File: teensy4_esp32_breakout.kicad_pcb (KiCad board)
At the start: 2 copper layers, 30.5 x 22.9 mm, 16 parts, among them J1 Conn_01x08, J2 Conn_02x05_Odd_Even, SW1 ON_OFF, U1 ESP32-WROOM-32D, U2 TLV75533PDBV

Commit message: Forgot to save
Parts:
- renumbered 3.3v to JP1
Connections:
- U1 pad 39: GND -> (no net)
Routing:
- net GND: vias 10 -> 9
- net /SCK: vias 2 -> 1
- net (no net): vias 0 -> 1

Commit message: Ordered this board with fix to remove double via and ground the BFV under ESP32
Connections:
- U1 pad 39: (no net) -> GND
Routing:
- net GND: vias 9 -> 10
- net (no net): vias 1 -> 0
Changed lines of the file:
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@@
     (fp_line (start -9.12 -15.865) (end -9.12 -9.445) (layer F.SilkS) (width 0.12))
     (fp_line (start -9.12 -9.445) (end -9.5 -9.445) (layer F.SilkS) (width 0.12))
-    (pad 39 smd rect (at -1 -0.755 270) (size 5 5) (layers F.Cu F.Paste F.Mask))
+    (pad 39 smd rect (at -1 -0.755 270) (size 5 5) (layers F.Cu F.Paste F.Mask)
+      (net 1 GND))
     (pad 1 smd rect (at -8.5 -8.255 270) (size 2 0.9) (layers F.Cu F.Paste F.Mask)
       (net 1 GND))
@@
   (gr_line (start 181.61 100.33) (end 181.61 123.19) (layer Edge.Cuts) (width 0.05))
   (gr_line (start 151.13 100.33) (end 181.61 100.33) (layer Edge.Cuts) (width 0.05))
-  (via (at 173.228 112.014) (size 4.318) (drill 3.81) (layers F.Cu B.Cu) (net 0) (status 30))
+  (via (at 173.228 112.014) (size 4.318) (drill 3.81) (layers F.Cu B.Cu) (net 1) (status 30))
   (segment (start 154.94 101.6) (end 155.067 101.6) (width 0.4572) (layer B.Cu) (net 1) (status 30))
   (segment (start 156.337 102.997) (end 154.94 101.6) (width 0.4572) (layer B.Cu) (net 1) (status 20))

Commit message: fix regulator part number
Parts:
- U2: value TLV75533PDBV -> TLV75733PDBVR
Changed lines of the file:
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@@
     (46 B.CrtYd user)
     (47 F.CrtYd user)
-    (48 B.Fab user hide)
-    (49 F.Fab user hide)
+    (48 B.Fab user)
+    (49 F.Fab user)
   )
   (setup
@@
     (add_net /MISO)
     (add_net /MOSI)
+    (add_net /PROGRAM)
     (add_net /SCK)
     (add_net GND)
@@
     (add_net "Net-(R2-Pad2)")
     (add_net "Net-(R3-Pad2)")
+    (add_net "Net-(U1-Pad14)")
+    (add_net "Net-(U1-Pad16)")
+    (add_net "Net-(U1-Pad17)")
+    (add_net "Net-(U1-Pad18)")
+    (add_net "Net-(U1-Pad19)")
+    (add_net "Net-(U1-Pad20)")
+    (add_net "Net-(U1-Pad21)")
+    (add_net "Net-(U1-Pad22)")
+    (add_net "Net-(U1-Pad23)")
+    (add_net "Net-(U1-Pad26)")
+    (add_net "Net-(U1-Pad27)")
+    (add_net "Net-(U1-Pad28)")
+    (add_net "Net-(U1-Pad31)")
+    (add_net "Net-(U1-Pad32)")
+    (add_net "Net-(U1-Pad33)")
+    (add_net "Net-(U1-Pad4)")
+    (add_net "Net-(U1-Pad5)")
+    (add_net "Net-(U1-Pad6)")
+    (add_net "Net-(U1-Pad7)")
+    (add_net "Net-(U1-Pad8)")
+    (add_net "Net-(U1-Pad9)")
+    (add_net "Net-(U2-Pad4)")
   )
   (module RF_Module:ESP32-WROOM-32 (layer F.Cu)
@@
       (effects (font (size 1 1) (thickness 0.15)))
     )
-    (fp_text value TLV75533PDBV (at 0 2.9) (layer F.Fab)
-      (effects (font (size 1 1) (thickness 0.15)))
-    )
+    (fp_text value TLV75733PDBVR (at 0 2.9) (layer F.Fab)
+      (effects (font (size 1 1) (thickness 0.15)))
+    )

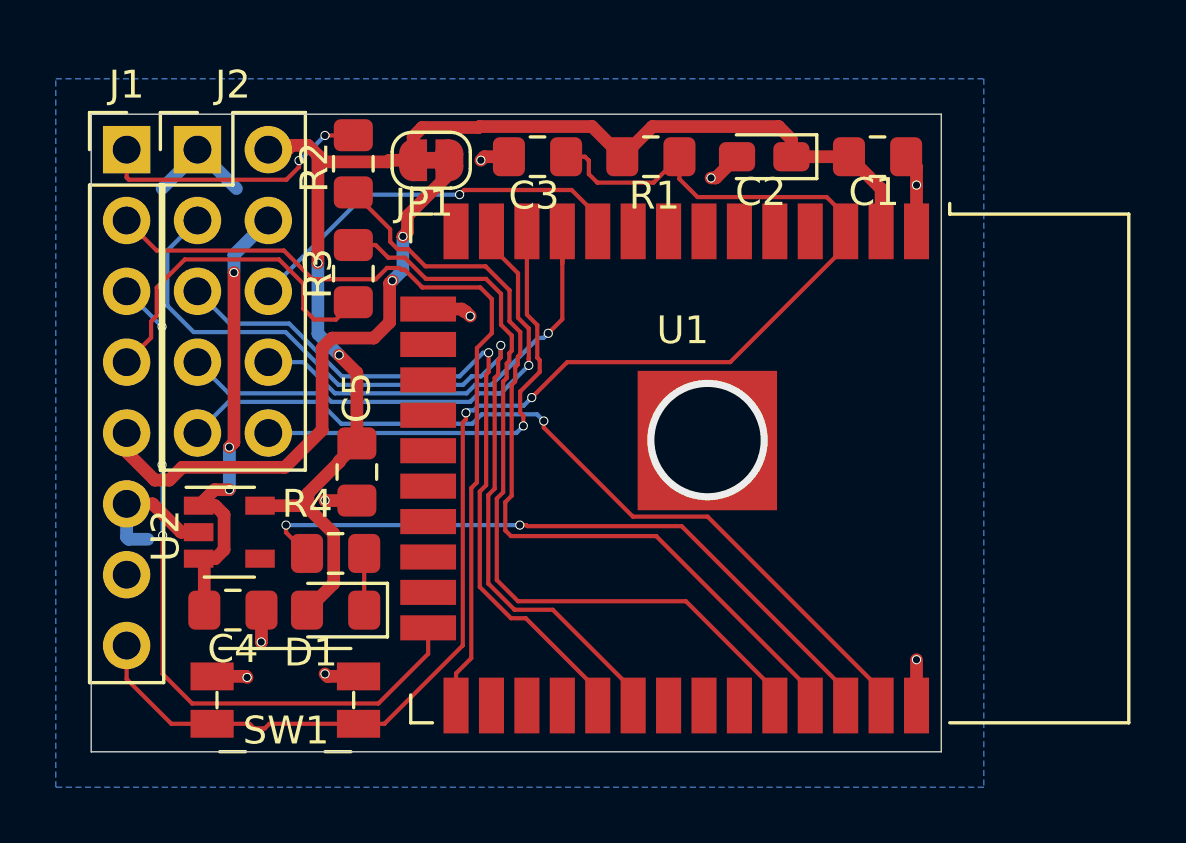
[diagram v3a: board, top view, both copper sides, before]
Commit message: Added two more pins from ESP32 to header, including pin used for ESP_BUSY by WiFiNINA
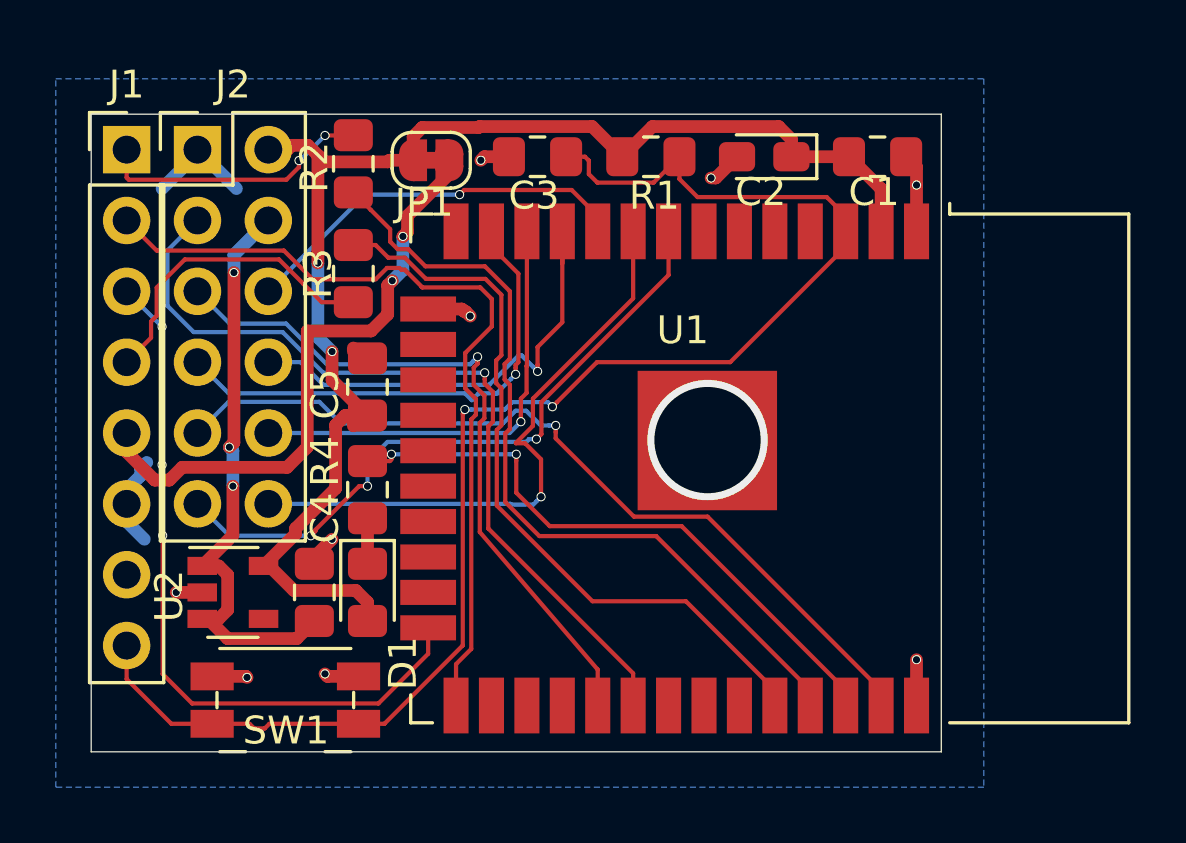
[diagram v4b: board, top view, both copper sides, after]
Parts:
- J2: value Conn_02x05_Odd_Even -> Conn_02x06_Odd_Even; footprint Connector_PinHeader_2.54mm:PinHeader_2x05_P2.54mm_Vertical -> Connector_PinHeader_2.54mm:PinHeader_2x06_P2.54mm_Vertical
- moved C5 3.07 mm to (161.0, 110.1), turned to 90 degrees
- moved C4 2.99 mm to (159.1, 117.5), turned to 90 degrees
- moved R4 2.56 mm to (161.0, 113.8), turned to 270 degrees
- moved U2 2.16 mm to (156.2, 117.5)
- moved D1 1.31 mm to (161.0, 117.5), turned to 270 degrees
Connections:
- U1 pad 8: (no net) -> /ESP_BUSY
- U1 pad 9: (no net) -> /IO33
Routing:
- net /ESP_BUSY: track 0.00 -> 24.0 mm, vias 0 -> 3
- net /IO33: track 0.00 -> 21.7 mm, vias 0 -> 1
- net /+5V: track 16.8 -> 21.4 mm
- net /SCK: track 33.5 -> 30.1 mm
- net +3V3: track 47.1 -> 49.8 mm
- net /IO22: track 24.4 -> 22.2 mm
- net Net-(R3-Pad2): track 28.8 -> 27.1 mm
- net /CS: track 26.9 -> 25.6 mm
- net GND: track 22.7 -> 21.6 mm
- net /24_TX6: track 12.3 -> 11.2 mm
- net /IO26: track 16.6 -> 17.4 mm
- net Net-(R2-Pad2): track 30.2 -> 29.4 mm
- net /IO27: track 16.8 -> 16.1 mm
- net /3V3_Teensy: track 21.3 -> 21.8 mm
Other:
- board text added: "3.3v 5v IO25 IO26 IO27 NC"
- board text added: "GND SCK CS MOSI MISO BUSY"
- board text added: "RX6 IO0 IO2 TX6 3.3v GND PGM ON/OFF"
- board text removed: "3.3v 5v IO25 IO26 IO27"
- board text removed: "GND SCK CS MOSI MISO"
- board text removed: "RX6 IO0 IO2 TX6 3.3v GND NC ON/OFF"

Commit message: Forgot to save
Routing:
- net /IO26: track 17.4 -> 16.6 mm
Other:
- board text added: "3.3v 5v IO25 IO26 IO27 IO33"
- board text added: "Teensy 4.0 ESP32 Breakout 2019-09-25"
- board text removed: "3.3v 5v IO25 IO26 IO27 NC"
- board text removed: "Teensy 4.0 ESP32 Breakout 2019-09-24"

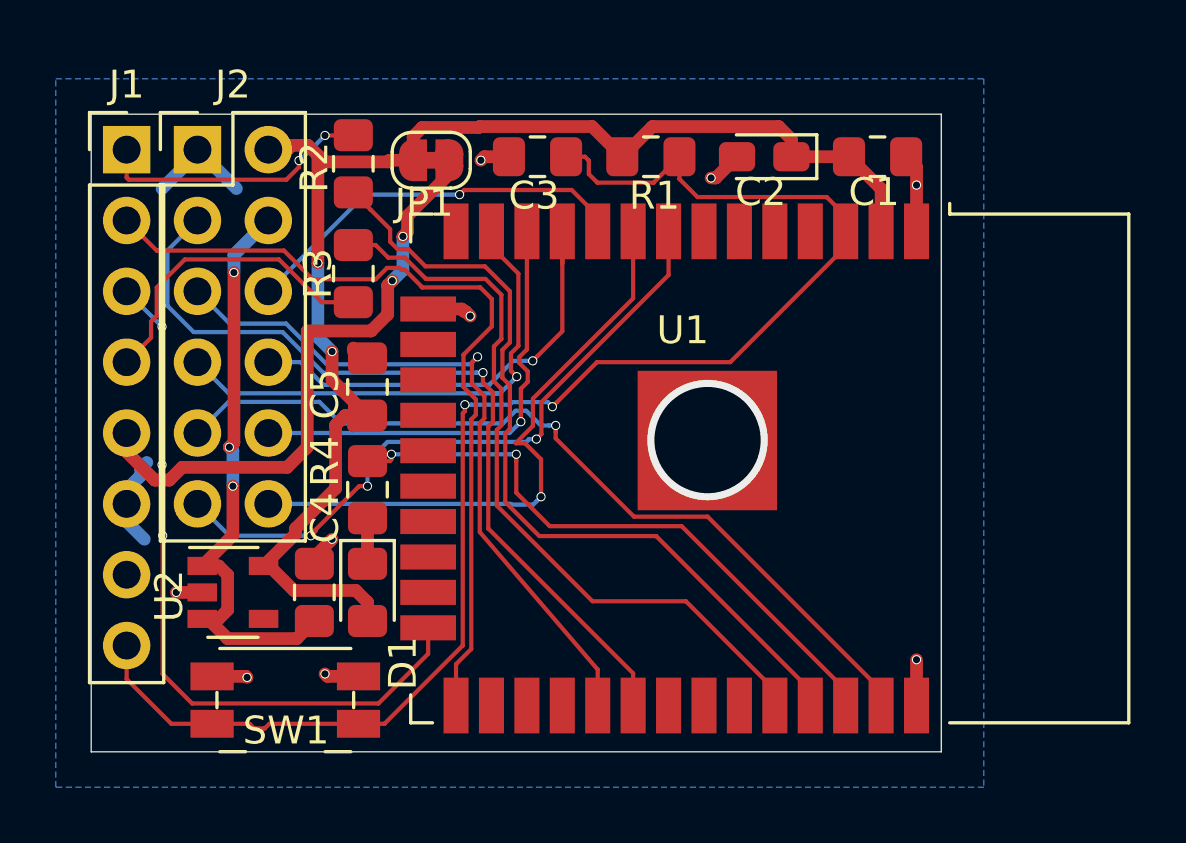
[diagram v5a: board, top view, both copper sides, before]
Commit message: Fix missing wire, update silkscreen & readme
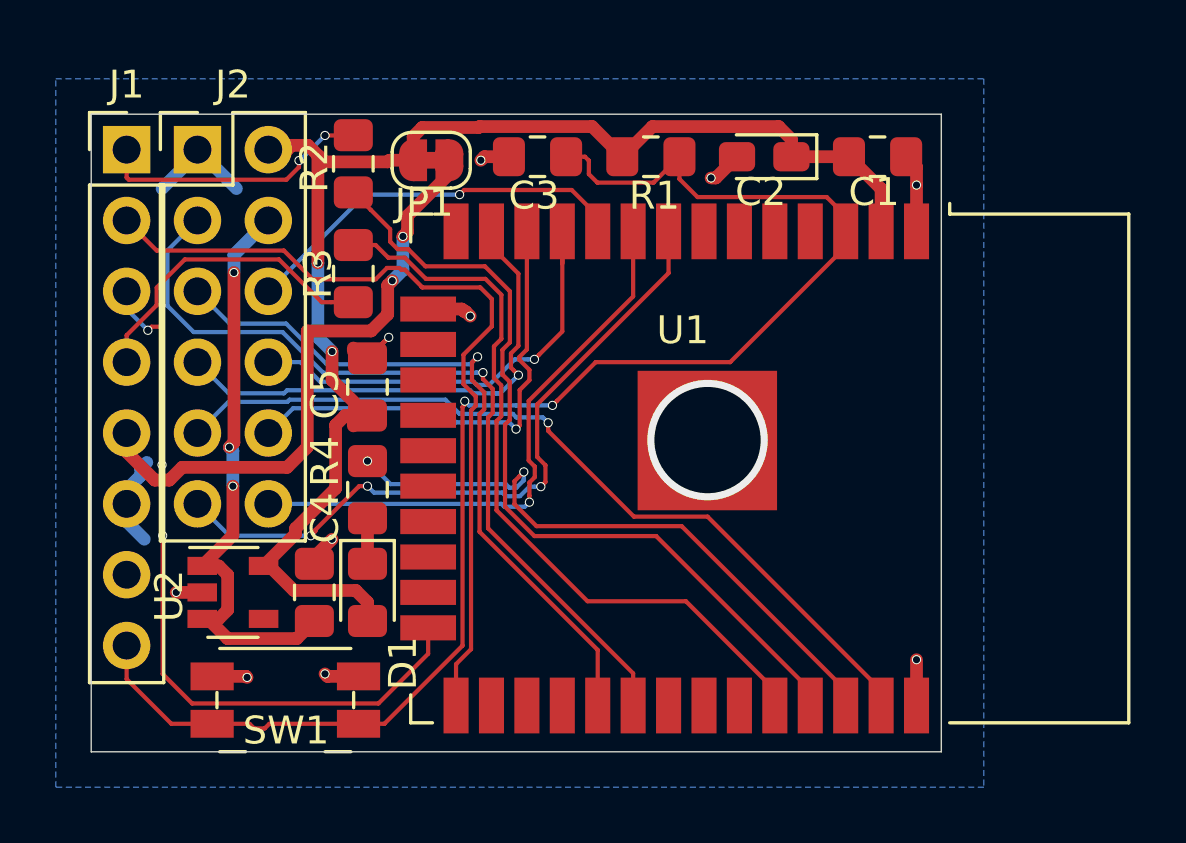
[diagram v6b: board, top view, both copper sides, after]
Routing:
- net GND: track 21.6 -> 24.1 mm, vias 10 -> 11
- net /ESP_BUSY: track 24.0 -> 25.1 mm
- net /IO33: track 21.7 -> 20.9 mm
- net /IO27: track 16.4 -> 17.1 mm
- net /IO22: track 22.2 -> 22.9 mm
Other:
- board text added: "RX6 IO0 IO2 TX6 3.3v GND PGM RESET"
- board text removed: "RX6 IO0 IO2 TX6 3.3v GND PGM ON/OFF"

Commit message: Updates to remove program/on_off pin connections
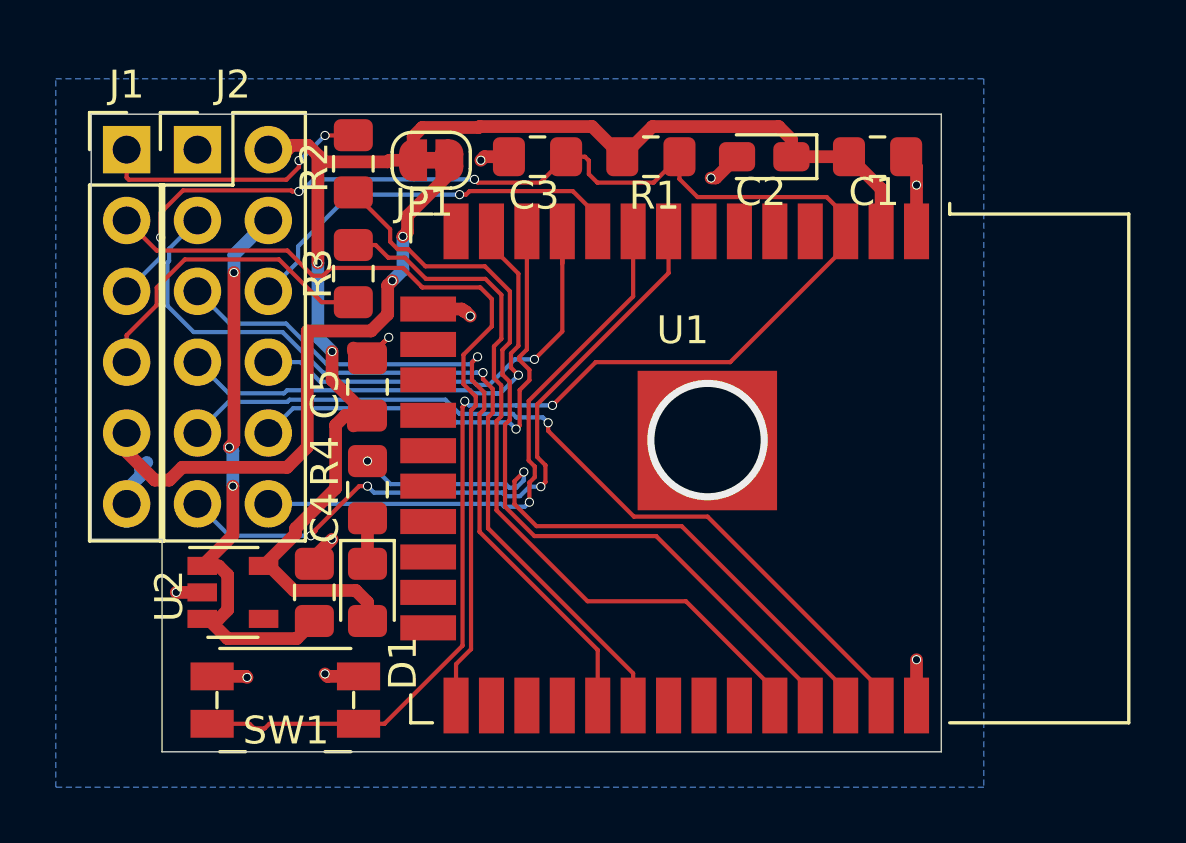
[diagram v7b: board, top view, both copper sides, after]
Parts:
- J1: value Conn_01x08 -> Conn_01x06; footprint Connector_PinHeader_2.54mm:PinHeader_1x08_P2.54mm_Vertical -> Connector_PinHeader_2.54mm:PinHeader_1x06_P2.54mm_Vertical
- SW1: value ON_OFF -> RESET
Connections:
- net /26 renamed /26_IO0
- C3 pad 1: /ESP32_EN -> /28_EN
- J1 pad 3: /28 -> /28_EN
- R1 pad 1: /ESP32_EN -> /28_EN
- SW1 pad 1: /ESP32_EN -> /28_EN
- U1 pad 24: /28 -> (no net)
- U1 pad 3: /ESP32_EN -> /28_EN
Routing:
- net /28_EN: track 0.00 -> 67.9 mm, vias 0 -> 5
- net /ESP32_EN: track 53.6 -> 0.00 mm, vias 2 -> 0
- net /28: track 26.4 -> 0.00 mm, vias 3 -> 0
- net GND: track 24.1 -> 19.4 mm
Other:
- outline, holes or cut-outs redrawn
- board text added: "3.3v out 5v in IO25 IO26 IO27 IO33"
- board text added: "RX6 IO0 EN TX6 3.3v GND"
- board text added: "Teensy 4.0 ESP32 Sidecar 2019-10-11"
- board text removed: "3.3v 5v IO25 IO26 IO27 IO33"
- board text removed: "RX6 IO0 IO2 TX6 3.3v GND PGM RESET"
- board text removed: "Teensy 4.0 ESP32 Breakout 2019-09-25"
